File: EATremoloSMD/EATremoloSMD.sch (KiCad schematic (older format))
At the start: 38 parts, among them J1 JACK__MONO_2P_NC, J2 BARREL_JACK, J3 JACK__MONO_2P_NC, Q1 Q_NJFET_DSG, Q2 Q_NPN_EBC, Q3 Q_NPN_EBC, Q4 Q_NJFET_DSG, SW1 SW_3PDT_on_on

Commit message: Created EATremoloSMD
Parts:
- C1, C2, C3, C4, C6, C8: footprint C_Disc_2mmPads:C_Disc_2mmPads -> Capacitors_SMD:C_0402_NoSilk
- C5, C7: footprint C_Disc_P5:C_Disc_P5.0mm_2mmPads -> Capacitors_SMD:C_0402_NoSilk
- C9: footprint CP_Radial_D4_P2_PadSize2_Drill1:CP_Radial_D4_P2_PadSize2_Drill1 -> Capacitors_SMD:C_0402_NoSilk
- D2: footprint Diodes_THT:D_DO-41_SOD81_P2.54mm_Vertical_AnodeUp -> Diodes_SMD:D_SOT-23_ANK
- Q2, Q3: footprint Q_NPN_EBC_PadSize2_Drill1:TO-92_Inline_Wide -> TO_SOT_Packages_SMD:SOT-23_Handsoldering
- R1, R10, R12, R13, R14, R15, R16, R2, R3, R4, R6, R7, R8, R9: footprint R_Axial_DIN0207_Vertical_2mmPad:R_Axial_DIN0207_Vertical_2mmPad -> Resistors_SMD:R_0402_NoSilk
- R11, R5: footprint R_Axial_DIN0207_P5:R_Axial_DIN0207_P5.08mm_2mmPads -> Resistors_SMD:R_0402_NoSilk
- RATE1, VOL1: footprint Potentiometers:Potentiometer_Omeg_PC16PU_Horizontal -> Potentiometers:Potentiometer_Bourns_PTV09A-1_Horizontal
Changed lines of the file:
@@
 EESchema Schematic File Version 2
-LIBS:EATremolo-rescue
 LIBS:power
 LIBS:device
@@
 LIBS:switches
 LIBS:sw_custom
-LIBS:EATremolo-cache
+LIBS:EATremoloSMD-cache
 EELAYER 25 0
 EELAYER END
@@
 F 0 "Q3" H 6050 2850 50  0000 L CNN
 F 1 "Q_NPN_EBC" H 6300 2650 50  0001 L CNN
-F 2 "Q_NPN_EBC_PadSize2_Drill1:TO-92_Inline_Wide" H 6300 2800 50  0001 C CNN
+F 2 "TO_SOT_Packages_SMD:SOT-23_Handsoldering" H 6300 2800 50  0001 C CNN
 F 3 "" H 6100 2700 50  0001 C CNN
 	1    6100 2700
@@
 F 0 "Q2" H 5950 6150 50  0000 L CNN
 F 1 "Q_NPN_EBC" H 5950 6050 50  0001 L CNN
-F 2 "Q_NPN_EBC_PadSize2_Drill1:TO-92_Inline_Wide" H 5950 6200 50  0001 C CNN
+F 2 "TO_SOT_Packages_SMD:SOT-23_Handsoldering" H 5950 6200 50  0001 C CNN
 F 3 "" H 5750 6100 50  0001 C CNN
 	1    5750 6100
@@
 F 0 "R1" H 3400 2050 50  0000 C CNN
 F 1 "1M" H 3400 2150 50  0000 C CNN
-F 2 "R_Axial_DIN0207_Vertical_2mmPad:R_Axial_DIN0207_Vertical_2mmPad" V 3180 2100 50  0001 C CNN
+F 2 "Resistors_SMD:R_0402_NoSilk" V 3180 2100 50  0001 C CNN
 F 3 "" H 3250 2100 50  0001 C CNN
 	1    3250 2100
@@
 F 0 "R3" H 4350 3400 50  0000 C CNN
 F 1 "1M" H 4350 3500 50  0000 C CNN
-F 2 "R_Axial_DIN0207_Vertical_2mmPad:R_Axial_DIN0207_Vertical_2mmPad" V 4130 3450 50  0001 C CNN
+F 2 "Resistors_SMD:R_0402_NoSilk" V 4130 3450 50  0001 C CNN
 F 3 "" H 4200 3450 50  0001 C CNN
 	1    4200 3450
@@
 F 0 "C1" V 3550 2950 50  0000 L CNN
 F 1 "47nF" V 3850 2950 50  0000 L CNN
-F 2 "C_Disc_2mmPads:C_Disc_2mmPads" H 3738 2850 50  0001 C CNN
+F 2 "Capacitors_SMD:C_0402_NoSilk" H 3738 2850 50  0001 C CNN
 F 3 "" H 3700 3000 50  0001 C CNN
 	1    3700 3000
@@
 F 0 "R2" H 4350 2350 50  0000 C CNN
 F 1 "1M" H 4350 2450 50  0000 C CNN
-F 2 "R_Axial_DIN0207_Vertical_2mmPad:R_Axial_DIN0207_Vertical_2mmPad" V 4130 2400 50  0001 C CNN
+F 2 "Resistors_SMD:R_0402_NoSilk" V 4130 2400 50  0001 C CNN
 F 3 "" H 4200 2400 50  0001 C CNN
 	1    4200 2400
@@
 F 0 "R5" H 4550 3500 50  0000 C CNN
 F 1 "10K" H 4550 3400 50  0000 C CNN
-F 2 "R_Axial_DIN0207_P5:R_Axial_DIN0207_P5.08mm_2mmPads" V 4630 3450 50  0001 C CNN
+F 2 "Resistors_SMD:R_0402_NoSilk" V 4630 3450 50  0001 C CNN
 F 3 "" H 4700 3450 50  0001 C CNN
 	1    4700 3450
@@
 F 0 "C5" V 5300 2700 50  0000 L CNN
 F 1 "10uF" V 5000 2650 50  0000 L CNN
-F 2 "C_Disc_P5:C_Disc_P5.0mm_2mmPads" H 5188 2550 50  0001 C CNN
+F 2 "Capacitors_SMD:C_0402_NoSilk" H 5188 2550 50  0001 C CNN
 F 3 "" H 5150 2700 50  0001 C CNN
 	1    5150 2700
@@
 F 0 "C6" V 5400 2650 50  0000 L CNN
 F 1 "220nF" V 5700 2600 50  0000 L CNN
-F 2 "C_Disc_2mmPads:C_Disc_2mmPads" H 5588 2550 50  0001 C CNN
+F 2 "Capacitors_SMD:C_0402_NoSilk" H 5588 2550 50  0001 C CNN
 F 3 "" H 5550 2700 50  0001 C CNN
 	1    5550 2700
@@
 F 0 "R8" H 5650 3500 50  0000 C CNN
 F 1 "150K" H 5650 3400 50  0000 C CNN
-F 2 "R_Axial_DIN0207_Vertical_2mmPad:R_Axial_DIN0207_Vertical_2mmPad" V 5730 3450 50  0001 C CNN
+F 2 "Resistors_SMD:R_0402_NoSilk" V 5730 3450 50  0001 C CNN
 F 3 "" H 5800 3450 50  0001 C CNN
 	1    5800 3450
@@
 F 0 "R10" V 6280 2150 50  0000 C CNN
 F 1 "4.7K" V 6200 2150 50  0000 C CNN
-F 2 "R_Axial_DIN0207_Vertical_2mmPad:R_Axial_DIN0207_Vertical_2mmPad" V 6130 2150 50  0001 C CNN
+F 2 "Resistors_SMD:R_0402_NoSilk" V 6130 2150 50  0001 C CNN
 F 3 "" H 6200 2150 50  0001 C CNN
 	1    6200 2150
@@
 F 0 "R7" V 5880 2250 50  0000 C CNN
 F 1 "560K" V 5800 2250 50  0000 C CNN
-F 2 "R_Axial_DIN0207_Vertical_2mmPad:R_Axial_DIN0207_Vertical_2mmPad" V 5730 2250 50  0001 C CNN
+F 2 "Resistors_SMD:R_0402_NoSilk" V 5730 2250 50  0001 C CNN
 F 3 "" H 5800 2250 50  0001 C CNN
 	1    5800 2250
@@
 F 0 "R11" V 6750 3000 50  0000 C CNN
 F 1 "180R" V 6950 3000 50  0000 C CNN
-F 2 "R_Axial_DIN0207_P5:R_Axial_DIN0207_P5.08mm_2mmPads" V 6780 3000 50  0001 C CNN
+F 2 "Resistors_SMD:R_0402_NoSilk" V 6780 3000 50  0001 C CNN
 F 3 "" H 6850 3000 50  0001 C CNN
 	1    6850 3000
@@
 F 0 "R12" H 7250 3400 50  0000 C CNN
 F 1 "1.2K" H 7250 3500 50  0000 C CNN
-F 2 "R_Axial_DIN0207_Vertical_2mmPad:R_Axial_DIN0207_Vertical_2mmPad" V 7030 3450 50  0001 C CNN
+F 2 "Resistors_SMD:R_0402_NoSilk" V 7030 3450 50  0001 C CNN
 F 3 "" H 7100 3450 50  0001 C CNN
 	1    7100 3450
@@
 F 0 "C9" V 7500 3000 50  0000 L CNN
 F 1 "10uF" V 7200 3000 50  0000 L CNN
-F 2 "CP_Radial_D4_P2_PadSize2_Drill1:CP_Radial_D4_P2_PadSize2_Drill1" H 7388 2850 50  0001 C CNN
+F 2 "Capacitors_SMD:C_0402_NoSilk" H 7388 2850 50  0001 C CNN
 F 3 "" H 7350 3000 50  0001 C CNN
 	1    7350 3000
@@
 F 0 "C7" V 6400 2350 50  0000 L CNN
 F 1 "470nF" V 6700 2350 50  0000 L CNN
-F 2 "C_Disc_P5:C_Disc_P5.0mm_2mmPads" H 6588 2250 50  0001 C CNN
+F 2 "Capacitors_SMD:C_0402_NoSilk" H 6588 2250 50  0001 C CNN
 F 3 "" H 6550 2400 50  0001 C CNN
 	1    6550 2400
@@
 F 0 "VOL1" V 6825 2400 50  0000 C CNN
 F 1 "A25K" V 6900 2400 50  0000 C CNN
-F 2 "Potentiometers:Potentiometer_Omeg_PC16PU_Horizontal" H 7000 2400 50  0001 C CNN
+F 2 "Potentiometers:Potentiometer_Bourns_PTV09A-1_Horizontal" H 7000 2400 50  0001 C CNN
 F 3 "" H 7000 2400 50  0001 C CNN
 	1    7000 2400
@@
 F 0 "R13" V 8980 3550 50  0000 C CNN
 F 1 "68k" V 8900 3550 50  0000 C CNN
-F 2 "R_Axial_DIN0207_Vertical_2mmPad:R_Axial_DIN0207_Vertical_2mmPad" V 8830 3550 50  0001 C CNN
+F 2 "Resistors_SMD:R_0402_NoSilk" V 8830 3550 50  0001 C CNN
 F 3 "" H 8900 3550 50  0001 C CNN
 	1    8900 3550
@@
 F 0 "C8" V 6450 5300 50  0000 L CNN
 F 1 "470nF" V 6750 5250 50  0000 L CNN
-F 2 "C_Disc_2mmPads:C_Disc_2mmPads" H 6638 5200 50  0001 C CNN
+F 2 "Capacitors_SMD:C_0402_NoSilk" H 6638 5200 50  0001 C CNN
 F 3 "" H 6600 5350 50  0001 C CNN
 	1    6600 5350
@@
 F 0 "R6" V 5680 5350 50  0000 C CNN
 F 1 "2.2M" V 5600 5350 50  0000 C CNN
-F 2 "R_Axial_DIN0207_Vertical_2mmPad:R_Axial_DIN0207_Vertical_2mmPad" V 5530 5350 50  0001 C CNN
+F 2 "Resistors_SMD:R_0402_NoSilk" V 5530 5350 50  0001 C CNN
 F 3 "" H 5600 5350 50  0001 C CNN
 	1    5600 5350
@@
 F 0 "R9" H 6000 4550 50  0000 C CNN
 F 1 "10K" H 6000 4650 50  0000 C CNN
-F 2 "R_Axial_DIN0207_Vertical_2mmPad:R_Axial_DIN0207_Vertical_2mmPad" V 5780 4600 50  0001 C CNN
+F 2 "Resistors_SMD:R_0402_NoSilk" V 5780 4600 50  0001 C CNN
 F 3 "" H 5850 4600 50  0001 C CNN
 	1    5850 4600
@@
 F 0 "C3" V 4750 5650 50  0000 L CNN
 F 1 "1uF" V 4850 5650 50  0000 L CNN
-F 2 "C_Disc_2mmPads:C_Disc_2mmPads" H 5038 5550 50  0001 C CNN
+F 2 "Capacitors_SMD:C_0402_NoSilk" H 5038 5550 50  0001 C CNN
 F 3 "" H 5000 5700 50  0001 C CNN
 	1    5000 5700
@@
 F 0 "C4" V 4850 6050 50  0000 L CNN
 F 1 "1uF" V 4750 6050 50  0000 L CNN
-F 2 "C_Disc_2mmPads:C_Disc_2mmPads" H 5038 5950 50  0001 C CNN
+F 2 "Capacitors_SMD:C_0402_NoSilk" H 5038 5950 50  0001 C CNN
 F 3 "" H 5000 6100 50  0001 C CNN
 	1    5000 6100
@@
 F 0 "C2" H 4575 6000 50  0000 L CNN
 F 1 "1uF" H 4575 5800 50  0000 L CNN
-F 2 "C_Disc_2mmPads:C_Disc_2mmPads" H 4588 5750 50  0001 C CNN
+F 2 "Capacitors_SMD:C_0402_NoSilk" H 4588 5750 50  0001 C CNN
 F 3 "" H 4550 5900 50  0001 C CNN
 	1    4550 5900
@@
 F 0 "R4" H 4700 6300 50  0000 C CNN
 F 1 "15K" H 4700 6400 50  0000 C CNN
-F 2 "R_Axial_DIN0207_Vertical_2mmPad:R_Axial_DIN0207_Vertical_2mmPad" V 4480 6350 50  0001 C CNN
+F 2 "Resistors_SMD:R_0402_NoSilk" V 4480 6350 50  0001 C CNN
 F 3 "" H 4550 6350 50  0001 C CNN
 	1    4550 6350
@@
 F 0 "RATE1" V 3575 5700 50  0000 C CNN
 F 1 "B100K" V 3650 5700 50  0000 C CNN
-F 2 "Potentiometers:Potentiometer_Omeg_PC16PU_Horizontal" H 3750 5700 50  0001 C CNN
+F 2 "Potentiometers:Potentiometer_Bourns_PTV09A-1_Horizontal" H 3750 5700 50  0001 C CNN
 F 3 "" H 3750 5700 50  0001 C CNN
 	1    3750 5700
@@
 F 0 "D2" H 2650 5600 50  0000 C CNN
 F 1 "D_Schottky" H 2650 5400 50  0000 C CNN
-F 2 "Diodes_THT:D_DO-41_SOD81_P2.54mm_Vertical_AnodeUp" H 2650 5500 50  0001 C CNN
+F 2 "Diodes_SMD:D_SOT-23_ANK" H 2650 5500 50  0001 C CNN
 F 3 "" H 2650 5500 50  0001 C CNN
 	1    2650 5500
@@
 F 0 "R15" V 8580 3550 50  0000 C CNN
 F 1 "100K" V 8500 3550 50  0000 C CNN
-F 2 "R_Axial_DIN0207_Vertical_2mmPad:R_Axial_DIN0207_Vertical_2mmPad" V 8430 3550 50  0001 C CNN
+F 2 "Resistors_SMD:R_0402_NoSilk" V 8430 3550 50  0001 C CNN
 F 3 "" H 8500 3550 50  0001 C CNN
 	1    8500 3550
@@
 F 0 "R14" V 8130 3800 50  0000 C CNN
 F 1 "180K" V 8050 3800 50  0000 C CNN
-F 2 "R_Axial_DIN0207_Vertical_2mmPad:R_Axial_DIN0207_Vertical_2mmPad" V 7980 3800 50  0001 C CNN
+F 2 "Resistors_SMD:R_0402_NoSilk" V 7980 3800 50  0001 C CNN
 F 3 "" H 8050 3800 50  0001 C CNN
 	1    8050 3800
@@
 F 0 "R16" V 4330 5700 50  0000 C CNN
 F 1 "1K" V 4250 5700 50  0000 C CNN
-F 2 "R_Axial_DIN0207_Vertical_2mmPad:R_Axial_DIN0207_Vertical_2mmPad" V 4180 5700 50  0001 C CNN
+F 2 "Resistors_SMD:R_0402_NoSilk" V 4180 5700 50  0001 C CNN
 F 3 "" H 4250 5700 50  0001 C CNN
 	1    4250 5700

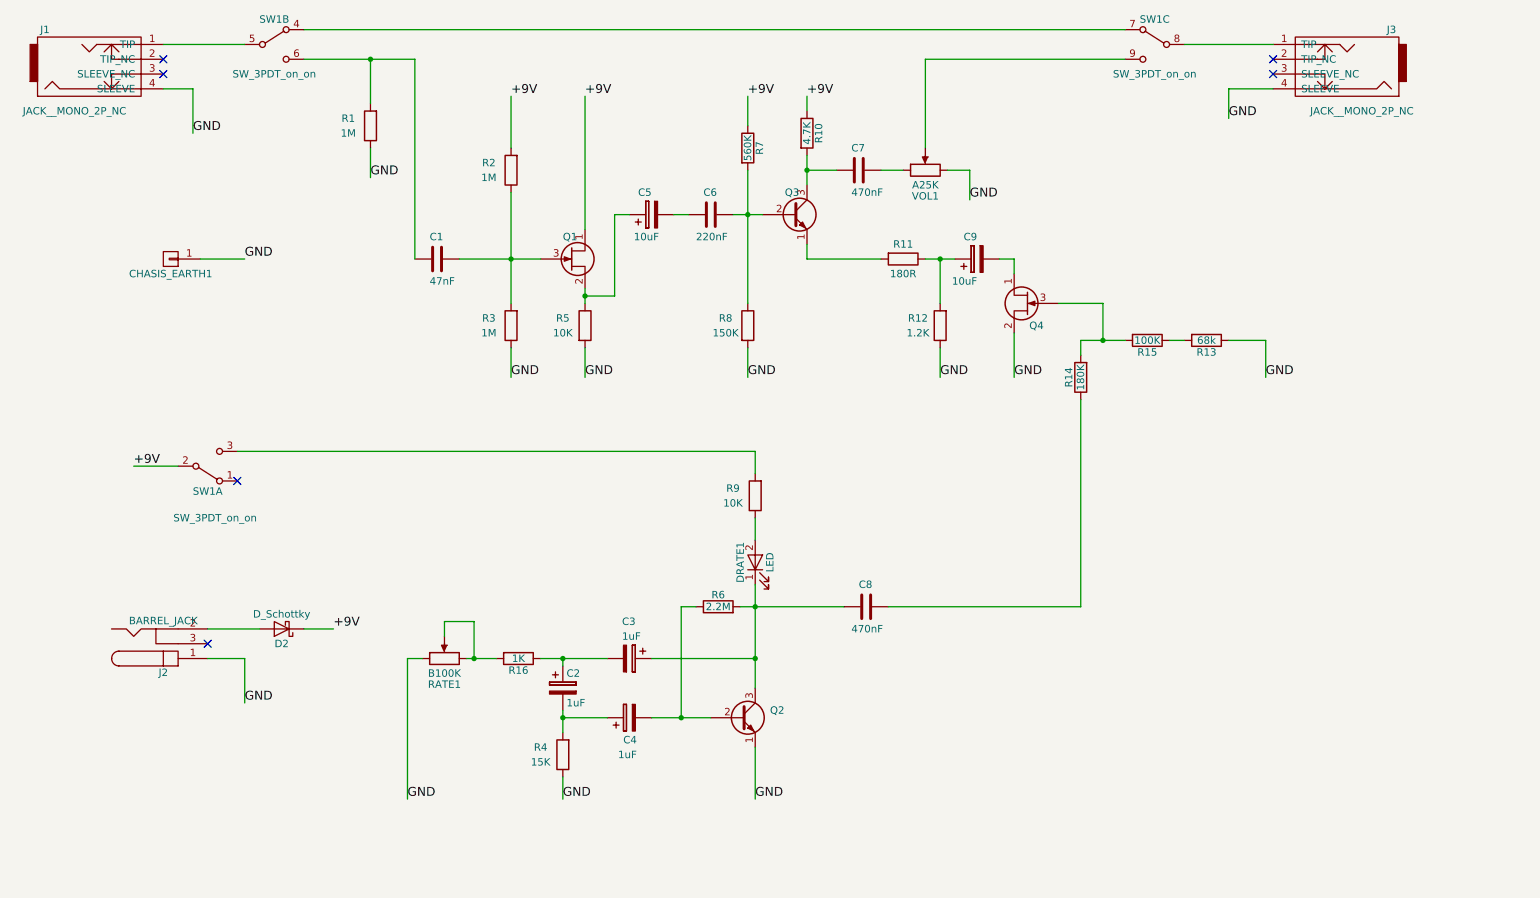
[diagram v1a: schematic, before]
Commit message: Updated EATremoloSMD
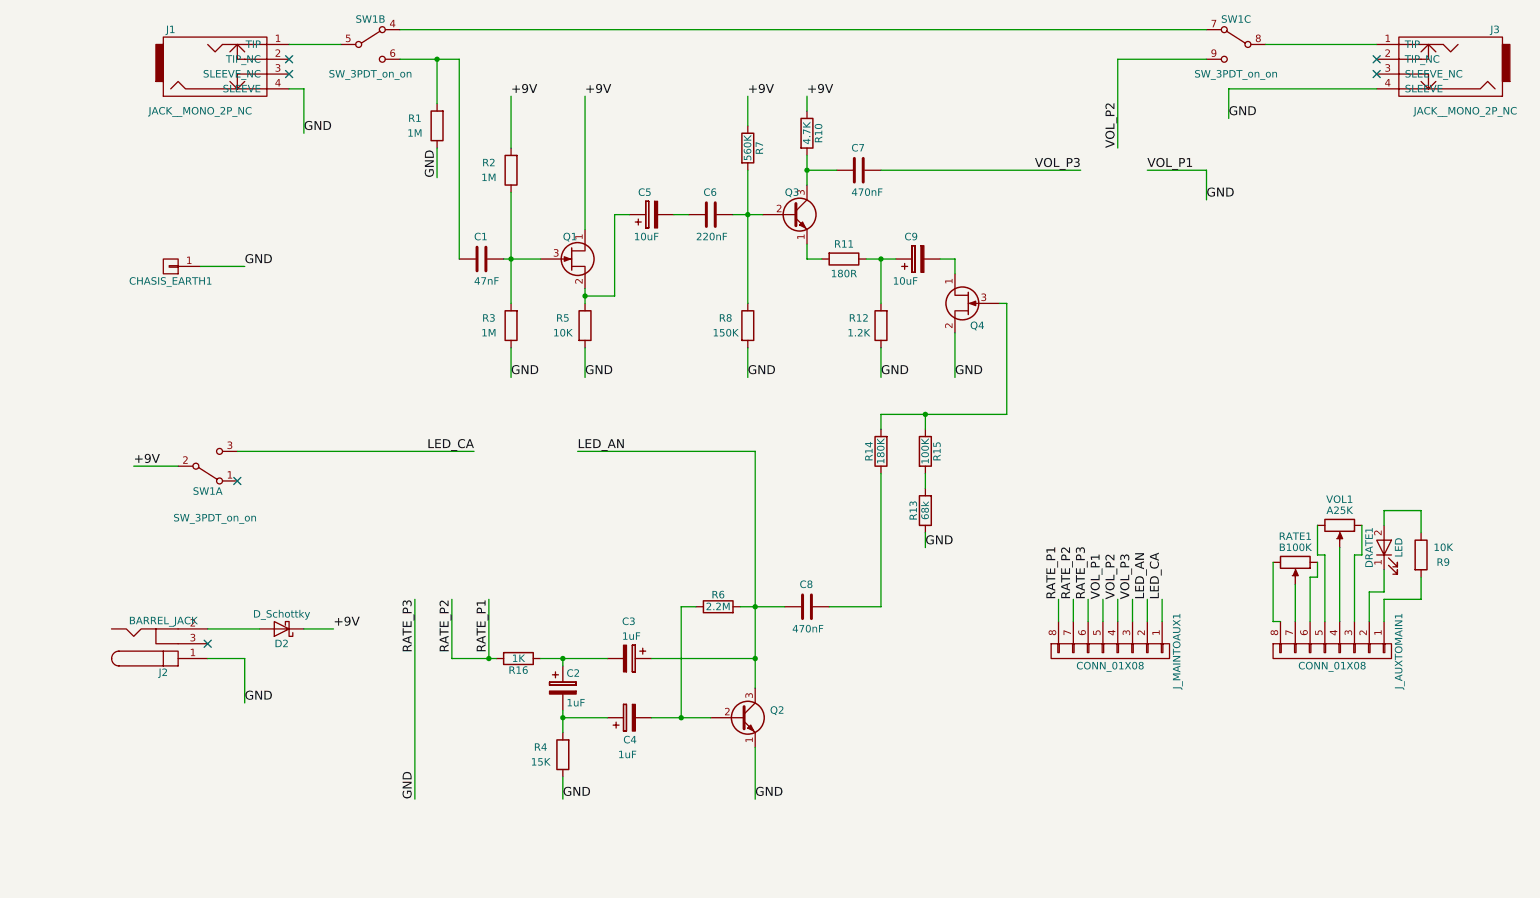
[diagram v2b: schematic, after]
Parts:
- added J_AUXTOMAIN1, J_MAINTOAUX1: CONN_01X08, Pin_Headers:Pin_Header_Straight_1x08_Pitch2.54mm, symbol CONN_01X08
- D2: footprint Diodes_SMD:D_SOT-23_ANK -> Diodes_SMD:D_SOD-323
- Q1, Q2, Q3, Q4: footprint TO_SOT_Packages_SMD:SOT-23_Handsoldering -> TO_SOT_Packages_SMD:SOT-23
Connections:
- net GND: now also J_MAINTOAUX1.5 (P5), J_MAINTOAUX1.6 (P6); no longer RATE1.1, VOL1.3
- net LED_AN: now reaches C3.1, C8.2, Q2.3 (C), R6.2
- net LED_AN: now also J_MAINTOAUX1.2 (P2); no longer DRATE1.1 (K)
- net at Q4.3 (G), R14.2: now also R15.1; no longer R15.2
- net at VOL1.1: now also J_AUXTOMAIN1.3 (P3); no longer C7.1
- net at VOL1.2: now also J_AUXTOMAIN1.4 (P4); no longer SW1.9 (C)
- net at R13.2: now also R15.2; no longer R15.1
- net at R9.2: now also J_AUXTOMAIN1.1 (P1); no longer SW1.3 (C)
- new net: J_AUXTOMAIN1.5 (P5), VOL1.3
- new net: J_AUXTOMAIN1.6 (P6), RATE1.1
- new net: J_AUXTOMAIN1.7 (P7), RATE1.2
- new net: J_AUXTOMAIN1.8 (P8), RATE1.3
- new net: DRATE1.1 (K), J_AUXTOMAIN1.2 (P2)
- new net LED_CA: J_MAINTOAUX1.1 (P1), SW1.3 (C)
- new net RATE_P1: J_MAINTOAUX1.7 (P7), J_MAINTOAUX1.8 (P8), R16.2
- new net VOL_P2: J_MAINTOAUX1.4 (P4), SW1.9 (C)
- new net VOL_P3: C7.1, J_MAINTOAUX1.3 (P3)
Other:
- moved on the sheet: C1, C8, C9, CHASIS_EARTH1, DRATE1, J1, J3, Q4, R1, R11, R12, R13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

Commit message: updates
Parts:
- SW1: footprint custom_sw:SW_3PDT_W18MM_L17.3MM_P5.3MM_D2MM -> custom_sw:SW_3PDT_W18MM_L17.3MM_P5.3MM_D2MM_SolderLugs
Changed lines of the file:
@@
 F 0 "SW1" H 3250 1720 50  0000 C CNN
 F 1 "SW_3PDT_on_on" H 3250 1350 50  0000 C CNN
-F 2 "custom_sw:SW_3PDT_W18MM_L17.3MM_P5.3MM_D2MM" H 3250 1550 50  0001 C CNN
+F 2 "custom_sw:SW_3PDT_W18MM_L17.3MM_P5.3MM_D2MM_SolderLugs" H 3250 1550 50  0001 C CNN
 F 3 "" H 3250 1550 50  0001 C CNN
 	2    3250 1550
@@
 F 0 "SW1" H 2150 4570 50  0000 C CNN
 F 1 "SW_3PDT_on_on" H 2200 4750 50  0000 C CNN
-F 2 "custom_sw:SW_3PDT_W18MM_L17.3MM_P5.3MM_D2MM" H 2150 4400 50  0001 C CNN
+F 2 "custom_sw:SW_3PDT_W18MM_L17.3MM_P5.3MM_D2MM_SolderLugs" H 2150 4400 50  0001 C CNN
 F 3 "" H 2150 4400 50  0001 C CNN
 	1    2150 4400
@@
 F 0 "SW1" H 9100 1720 50  0000 C CNN
 F 1 "SW_3PDT_on_on" H 9100 1350 50  0000 C CNN
-F 2 "custom_sw:SW_3PDT_W18MM_L17.3MM_P5.3MM_D2MM" H 9100 1550 50  0001 C CNN
+F 2 "custom_sw:SW_3PDT_W18MM_L17.3MM_P5.3MM_D2MM_SolderLugs" H 9100 1550 50  0001 C CNN
 F 3 "" H 9100 1550 50  0001 C CNN
 	3    9100 1550
